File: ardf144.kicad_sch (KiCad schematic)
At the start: 54 parts, among them J1 Jack-DC, Q1 2SC1906, SW1 SW_SPST, U1 NE612, U2 2SK439, U3 L7805, U4 LM386, U5 2SK439, Y1 16MHz

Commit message: second
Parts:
- added J2, J3: Conn_01x02_Socket, Connector_PinSocket_2.54mm:PinSocket_1x02_P2.54mm_Vertical, symbol Connector:Conn_01x02_Socket
- C9: footprint Capacitor_THT:C_Disc_D5.0mm_W2.5mm_P2.50mm -> Capacitor_THT:CP_Radial_D6.3mm_P2.50mm; symbol Device:C -> Device:C_Polarized
- J1: footprint Connector_BarrelJack:BarrelJack_Wuerth_694106106102_2.0x5.5mm -> Library:2.5jack
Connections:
- net 9v: now also RV1.3; no longer RV1.1
- net GND: now also RV1.1, J2.2 (Pin_2), J3.1 (Pin_1); no longer RV1.3
- net at C1.1: now also J3.2 (Pin_2)
- net at SW1.1 (A): now also J2.1 (Pin_1)

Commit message: fix 3
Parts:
- added C25: 0.1u, Capacitor_THT:C_Disc_D5.0mm_W2.5mm_P2.50mm, symbol Device:C
- added C26: 0.1u, Capacitor_THT:C_Disc_D5.0mm_W2.5mm_P5.00mm, symbol Device:C
- added C27: 0.047u, Capacitor_THT:C_Disc_D5.0mm_W2.5mm_P2.50mm, symbol Device:C
- D2: footprint Diode_THT:D_DO-41_SOD81_P10.16mm_Horizontal -> Diode_THT:D_DO-41_SOD81_P2.54mm_Vertical_AnodeUp
- J2: value Conn_01x02_Socket -> batt
- J3: value Conn_01x02_Socket -> ant
- R7: value R -> 10
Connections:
- net AF: now also C25.2, C27.1; no longer U1.4 (OUT_A)
- net GND: now also C26.2, C27.2
- net at U1.5 (OUT_B): now also C26.1
- new net: C25.1, U1.4 (OUT_A)
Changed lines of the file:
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@@
   (junction (at 55.88 105.41) (diameter 0) (color 0 0 0 0)
   )
+  (junction (at 113.03 67.31) (diameter 0) (color 0 0 0 0)
+  )
   (junction (at 45.72 118.11) (diameter 0) (color 0 0 0 0)
   )
@@
   (junction (at 114.3 40.64) (diameter 0) (color 0 0 0 0)
   )
+  (junction (at 95.25 67.31) (diameter 0) (color 0 0 0 0)
+  )
   (junction (at 57.15 33.02) (diameter 0) (color 0 0 0 0)
   )
@@
     (stroke (width 0) (type default))
   )
+  (wire (pts (xy 109.22 67.31) (xy 113.03 67.31))
+    (stroke (width 0) (type default))
+  )
   (wire (pts (xy 53.34 33.02) (xy 57.15 33.02))
     (stroke (width 0) (type default))
@@
     (stroke (width 0) (type default))
   )
+  (wire (pts (xy 113.03 67.31) (xy 113.03 66.04))
+    (stroke (width 0) (type default))
+  )
   (wire (pts (xy 46.99 68.58) (xy 53.34 68.58))
     (stroke (width 0) (type default))
@@
     (stroke (width 0) (type default))
   )
+  (wire (pts (xy 95.25 59.69) (xy 95.25 58.42))
+    (stroke (width 0) (type default))
+  )
   (wire (pts (xy 57.15 33.02) (xy 67.31 33.02))
     (stroke (width 0) (type default))
@@
     (stroke (width 0) (type default))
   )
+  (wire (pts (xy 95.25 68.58) (xy 95.25 67.31))
+    (stroke (width 0) (type default))
+  )
   (wire (pts (xy 45.72 95.25) (xy 55.88 95.25))
     (stroke (width 0) (type default))
   )
+  (wire (pts (xy 113.03 68.58) (xy 113.03 67.31))
+    (stroke (width 0) (type default))
+  )
   (wire (pts (xy 223.52 64.77) (xy 237.49 64.77))
     (stroke (width 0) (type default))
@@
   )
   (wire (pts (xy 96.52 97.79) (xy 106.68 97.79))
+    (stroke (width 0) (type default))
+  )
+  (wire (pts (xy 101.6 67.31) (xy 95.25 67.31))
     (stroke (width 0) (type default))
   )
@@
     )
   )
-  (global_label "AF" (shape output) (at 95.25 58.42 270) (fields_autoplaced)
+  (global_label "AF" (shape output) (at 95.25 68.58 270) (fields_autoplaced)
     (effects (font (size 1.27 1.27)) (justify right))
-    (property "Intersheetrefs" "${INTERSHEET_REFS}" (at 95.25 63.5824 90)
+    (property "Intersheetrefs" "${INTERSHEET_REFS}" (at 95.25 73.7424 90)
       (effects (font (size 1.27 1.27)) (justify right) hide)
     )
@@
       (effects (font (size 1.27 1.27)) (justify left))
     )
-    (property "Footprint" "Diode_THT:D_DO-41_SOD81_P10.16mm_Horizontal" (at 223.52 68.58 0)
+    (property "Footprint" "Diode_THT:D_DO-41_SOD81_P2.54mm_Vertical_AnodeUp" (at 223.52 68.58 0)
       (effects (font (size 1.27 1.27)) hide)
     )
@@
     )
     (property "Value" "GND" (at 93.98 53.34 90)
-      (effects (font (size 1.27 1.27)) (justify right))
+      (effects (font (size 1.27 1.27)) (justify right) hide)
     )
     (property "Footprint" "" (at 95.25 54.61 0)
@@
       (effects (font (size 1.27 1.27)))
     )
-    (property "Value" "R" (at 242.57 55.88 90)
+    (property "Value" "10" (at 242.57 55.88 90)
       (effects (font (size 1.27 1.27)))
     )
@@
       (effects (font (size 1.27 1.27)) (justify left))
     )
-    (property "Value" "Conn_01x02_Socket" (at 219.71 43.815 0)
+    (property "Value" "batt" (at 219.71 43.815 0)
       (effects (font (size 1.27 1.27)) (justify left))
     )
@@
         (path "/26813511-9f1f-4e27-8c3c-943dea9d773a"
           (reference "#PWR017") (unit 1)
+        )
+      )
+    )
+  )
+  (symbol (lib_id "Device:C") (at 105.41 67.31 90) (unit 1)
+    (in_bom yes) (on_board yes) (dnp no)
+    (property "Reference" "C27" (at 105.41 71.12 90)
+      (effects (font (size 1.27 1.27)))
+    )
+    (property "Value" "0.047u" (at 105.41 73.66 90)
+      (effects (font (size 1.27 1.27)))
+    )
+    (property "Footprint" "Capacitor_THT:C_Disc_D5.0mm_W2.5mm_P2.50mm" (at 109.22 66.3448 0)
+      (effects (font (size 1.27 1.27)) hide)
+    )
+    (property "Datasheet" "~" (at 105.41 67.31 0)
+      (effects (font (size 1.27 1.27)) hide)
+    )
+    (pin "2")
+    (pin "1")
+    (instances
+      (project "ardf144"
+        (path "/26813511-9f1f-4e27-8c3c-943dea9d773a"
+          (reference "C27") (unit 1)
         )
       )
@@
     )
   )
+  (symbol (lib_id "power:GND") (at 113.03 68.58 0) (unit 1)
+    (in_bom yes) (on_board yes) (dnp no) (fields_autoplaced)
+    (property "Reference" "#PWR033" (at 113.03 74.93 0)
+      (effects (font (size 1.27 1.27)) hide)
+    )
+    (property "Value" "GND" (at 113.03 73.66 0)
+      (effects (font (size 1.27 1.27)) hide)
+    )
+    (property "Footprint" "" (at 113.03 68.58 0)
+      (effects (font (size 1.27 1.27)) hide)
+    )
+    (property "Datasheet" "" (at 113.03 68.58 0)
+      (effects (font (size 1.27 1.27)) hide)
+    )
+    (pin "1")
+    (instances
+      (project "ardf144"
+        (path "/26813511-9f1f-4e27-8c3c-943dea9d773a"
+          (reference "#PWR033") (unit 1)
+        )
+      )
+    )
+  )
   (symbol (lib_id "Device:C") (at 116.84 54.61 90) (unit 1)
     (in_bom yes) (on_board yes) (dnp no)
@@
     )
   )
+  (symbol (lib_id "Device:C") (at 95.25 63.5 0) (unit 1)
+    (in_bom yes) (on_board yes) (dnp no) (fields_autoplaced)
+    (property "Reference" "C25" (at 99.06 62.23 0)
+      (effects (font (size 1.27 1.27)) (justify left))
+    )
+    (property "Value" "0.1u" (at 99.06 64.77 0)
+      (effects (font (size 1.27 1.27)) (justify left))
+    )
+    (property "Footprint" "Capacitor_THT:C_Disc_D5.0mm_W2.5mm_P2.50mm" (at 96.2152 67.31 0)
+      (effects (font (size 1.27 1.27)) hide)
+    )
+    (property "Datasheet" "~" (at 95.25 63.5 0)
+      (effects (font (size 1.27 1.27)) hide)
+    )
+    (pin "2")
+    (pin "1")
+    (instances
+      (project "ardf144"
+        (path "/26813511-9f1f-4e27-8c3c-943dea9d773a"
+          (reference "C25") (unit 1)
+        )
+      )
+    )
+  )
   (symbol (lib_id "power:GND") (at 33.02 125.73 0) (unit 1)
     (in_bom yes) (on_board yes) (dnp no) (fields_autoplaced)
@@
       (effects (font (size 1.27 1.27)))
     )
-    (property "Value" "Conn_01x02_Socket" (at 15.875 59.69 0)
+    (property "Value" "ant" (at 15.875 59.69 0)
       (effects (font (size 1.27 1.27)) hide)
     )
@@
         )
       )
+    )
+  )
+  (symbol (lib_id "Device:C") (at 113.03 62.23 0) (unit 1)
+    (in_bom yes) (on_board yes) (dnp no)
+    (property "Reference" "C26" (at 114.3 66.04 0)
+      (effects (font (size 1.27 1.27)) (justify left))
+    )
+    (property "Value" "0.1u" (at 114.3 68.58 0)
+      (effects (font (size 1.27 1.27)) (justify left))
+    )
+    (property "Footprint" "Capacitor_THT:C_Disc_D5.0mm_W2.5mm_P5.00mm" (at 113.9952 66.04 0)
+      (effects (font (size 1.27 1.27)) hide)
+    )
+    (property "Datasheet" "~" (at 113.03 62.23 0)
+      (effects (font (size 1.27 1.27)) hide)
+    )
+    (pin "2")
+    (pin "1")
+    (instances
+      (project "ardf144"
+        (path "/26813511-9f1f-4e27-8c3c-943dea9d773a"
+          (reference "C26") (unit 1)
+        )
+      )

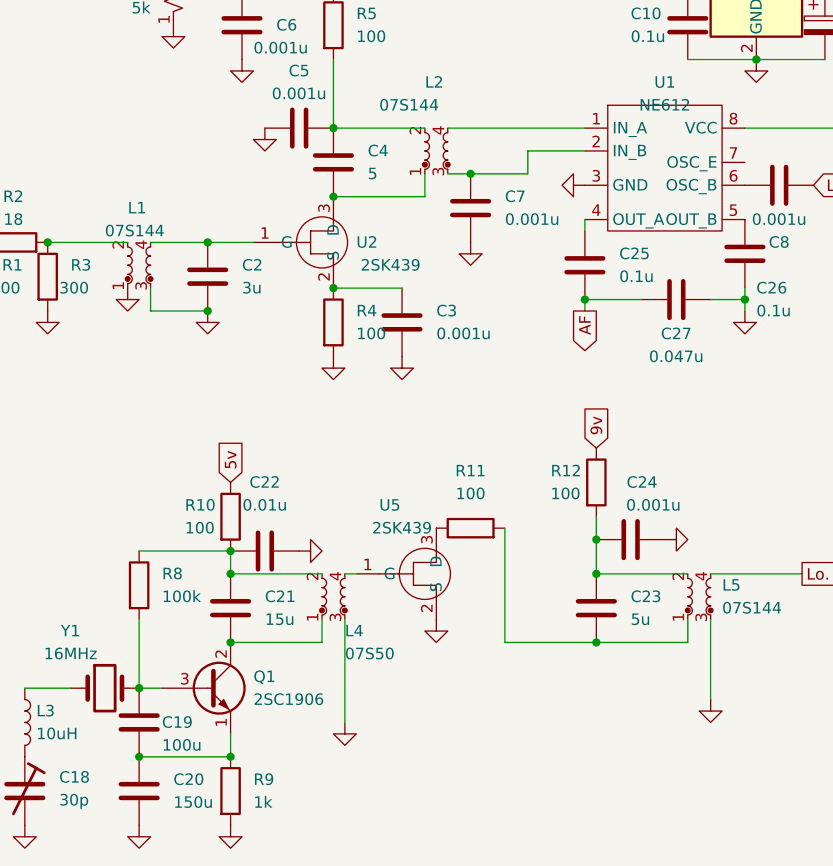
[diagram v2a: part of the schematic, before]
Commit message: fix capacitance
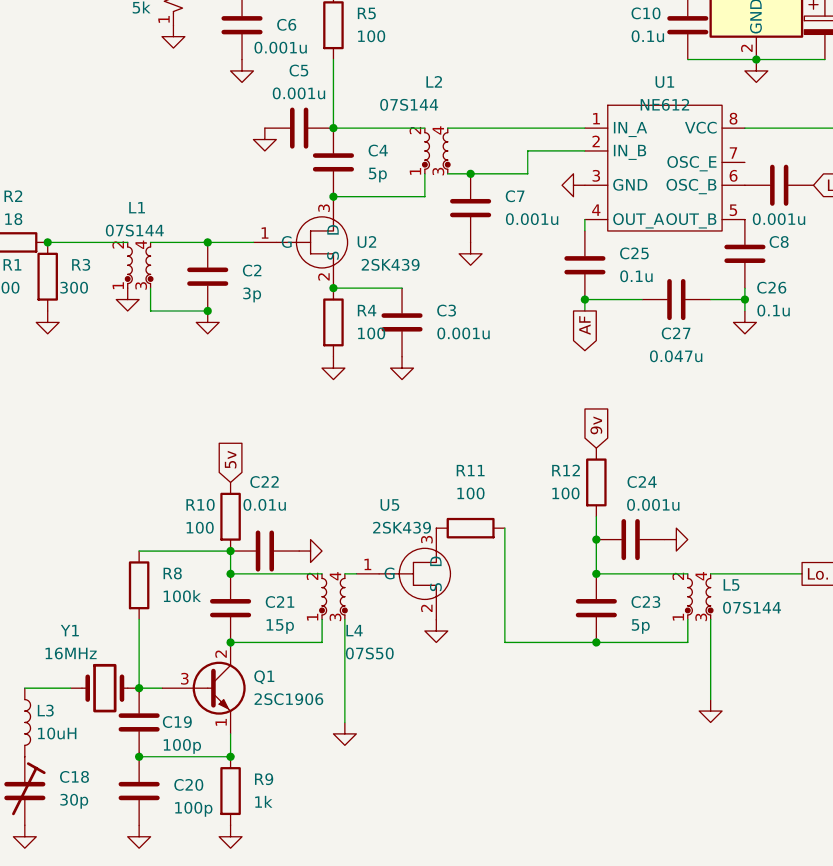
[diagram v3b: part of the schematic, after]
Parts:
- C19: value 100u -> 100p
- C2: value 3u -> 3p
- C20: value 150u -> 100p
- C21: value 15u -> 15p
- C23: value 5u -> 5p
- C4: value 5 -> 5p
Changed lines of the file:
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@@
       (effects (font (size 1.27 1.27)) (justify left))
     )
-    (property "Value" "100u" (at 48.26 116.84 0)
+    (property "Value" "100p" (at 48.26 116.84 0)
       (effects (font (size 1.27 1.27)) (justify left))
     )
@@
       (effects (font (size 1.27 1.27)) (justify left))
     )
-    (property "Value" "5" (at 71.12 53.34 0)
+    (property "Value" "5p" (at 71.12 53.34 0)
       (effects (font (size 1.27 1.27)) (justify left))
     )
@@
       (effects (font (size 1.27 1.27)) hide)
     )
-    (pin "2")
-    (pin "1")
+    (pin "1")
+    (pin "2")
     (instances
       (project "ardf144"
@@
   (symbol (lib_id "Device:C") (at 45.72 121.92 0) (unit 1)
     (in_bom yes) (on_board yes) (dnp no) (fields_autoplaced)
-    (property "Reference" "C20" (at 49.53 120.65 0)
-      (effects (font (size 1.27 1.27)) (justify left))
-    )
-    (property "Value" "150u" (at 49.53 123.19 0)
+    (property "Reference" "C20" (at 49.53 121.285 0)
+      (effects (font (size 1.27 1.27)) (justify left))
+    )
+    (property "Value" "100p" (at 49.53 123.825 0)
       (effects (font (size 1.27 1.27)) (justify left))
     )
@@
   (symbol (lib_id "Device:C") (at 96.52 101.6 0) (unit 1)
     (in_bom yes) (on_board yes) (dnp no) (fields_autoplaced)
-    (property "Reference" "C23" (at 100.33 100.33 0)
-      (effects (font (size 1.27 1.27)) (justify left))
-    )
-    (property "Value" "5u" (at 100.33 102.87 0)
+    (property "Reference" "C23" (at 100.33 100.965 0)
+      (effects (font (size 1.27 1.27)) (justify left))
+    )
+    (property "Value" "5p" (at 100.33 103.505 0)
       (effects (font (size 1.27 1.27)) (justify left))
     )
@@
       (effects (font (size 1.27 1.27)) hide)
     )
-    (pin "2")
-    (pin "1")
+    (pin "1")
+    (pin "2")
     (instances
       (project "ardf144"
@@
   (symbol (lib_id "Device:C") (at 55.88 101.6 0) (unit 1)
     (in_bom yes) (on_board yes) (dnp no) (fields_autoplaced)
-    (property "Reference" "C21" (at 59.69 100.33 0)
-      (effects (font (size 1.27 1.27)) (justify left))
-    )
-    (property "Value" "15u" (at 59.69 102.87 0)
+    (property "Reference" "C21" (at 59.69 100.965 0)
+      (effects (font (size 1.27 1.27)) (justify left))
+    )
+    (property "Value" "15p" (at 59.69 103.505 0)
       (effects (font (size 1.27 1.27)) (justify left))
     )
@@
   (symbol (lib_id "Device:C") (at 53.34 64.77 0) (unit 1)
     (in_bom yes) (on_board yes) (dnp no) (fields_autoplaced)
-    (property "Reference" "C2" (at 57.15 63.5 0)
-      (effects (font (size 1.27 1.27)) (justify left))
-    )
-    (property "Value" "3u" (at 57.15 66.04 0)
+    (property "Reference" "C2" (at 57.15 64.135 0)
+      (effects (font (size 1.27 1.27)) (justify left))
+    )
+    (property "Value" "3p" (at 57.15 66.675 0)
       (effects (font (size 1.27 1.27)) (justify left))
     )
@@
       (effects (font (size 1.27 1.27)) hide)
     )
-    (pin "2")
-    (pin "1")
-    (instances
-      (project "ardf144"
+    (pin "1")
+    (pin "2")
+    (instances
+      (project "ardf144"

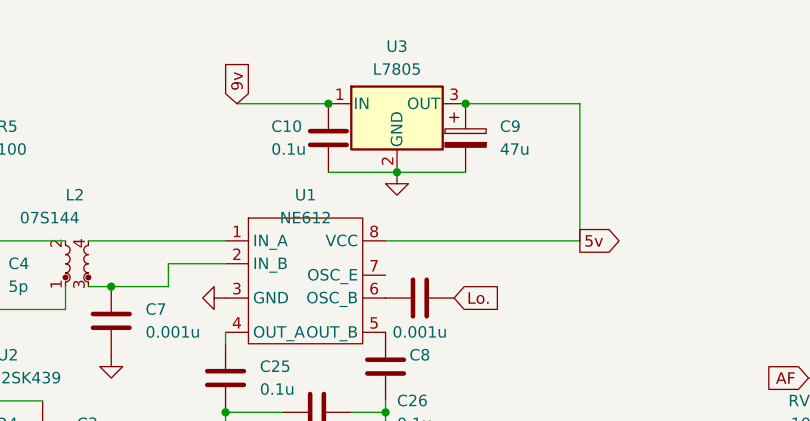
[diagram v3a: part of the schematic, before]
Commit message: fix attiny vcc +3v3 from +5v
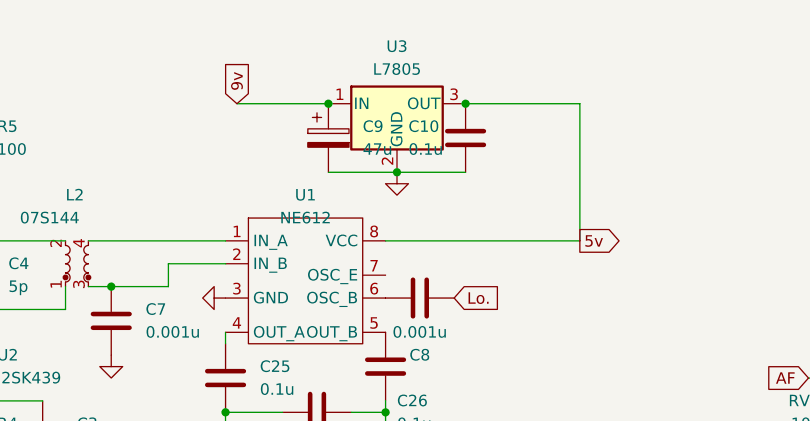
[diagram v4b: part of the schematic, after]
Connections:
- net 5v: now also C10.1; no longer C9.1
- net 9v: now also C9.1; no longer C10.1
